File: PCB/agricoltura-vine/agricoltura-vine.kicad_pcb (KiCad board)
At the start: 4 copper layers, 110 x 75 mm, 100 parts, among them SW1 TL3301NF260QG, T1 BU2032SM-JJ-GTR, T10 BM04B-SRSS-TB(LF)(SN), T11 BM04B-SRSS-TB(LF)(SN), T12 BM04B-SRSS-TB(LF)(SN), T13 BM04B-SRSS-TB(LF)(SN), T14 BM04B-SRSS-TB(LF)(SN), T15 BM04B-SRSS-TB(LF)(SN), T16 1757242, T17 0395121004, T18 0395121004, T19 TSW-108-07-G-T, T2 20021121-00010C4LF, T20 TSW-108-07-G-T, T3 0675031020, T4 BM04B-SRSS-TB(LF)(SN), T5 BM04B-SRSS-TB(LF)(SN), T6 BM04B-SRSS-TB(LF)(SN), T7 BM04B-SRSS-TB(LF)(SN), T8 BM04B-SRSS-TB(LF)(SN), T9 BM04B-SRSS-TB(LF)(SN), U1 STM32F446RET6, U2 74HC4052D, U3 TCA9548APWR, U4 AP63203WU-7, U5 AP63205WU-7, U6 MAX13450EAUD+, U7 MAX13450EAUD+, U8 SN74LV541APWR, U9 TXB0108PWR, X1 ABM3B-8.000MHZ-B2-T, X2 ABS07-32.768KHZ-9-T

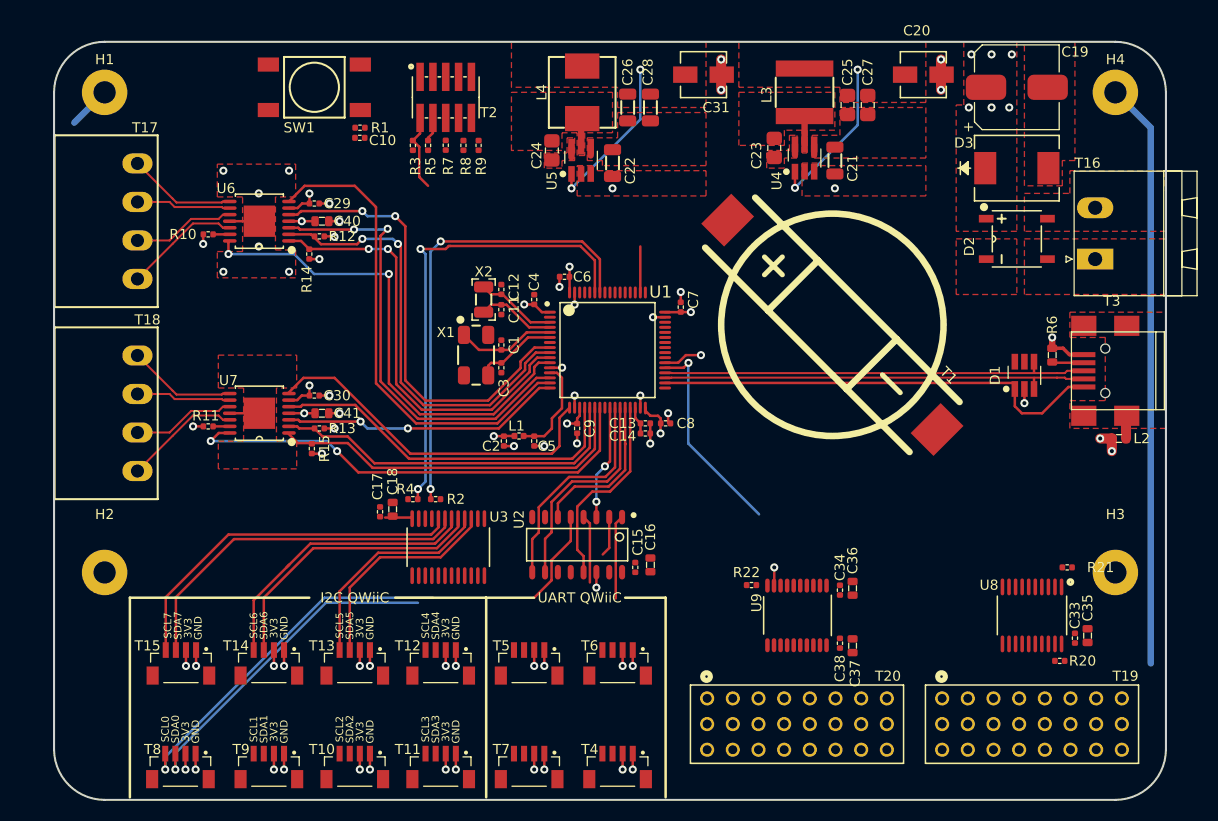
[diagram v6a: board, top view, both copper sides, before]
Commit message: IO Expander
added IO expander for 5V IOs
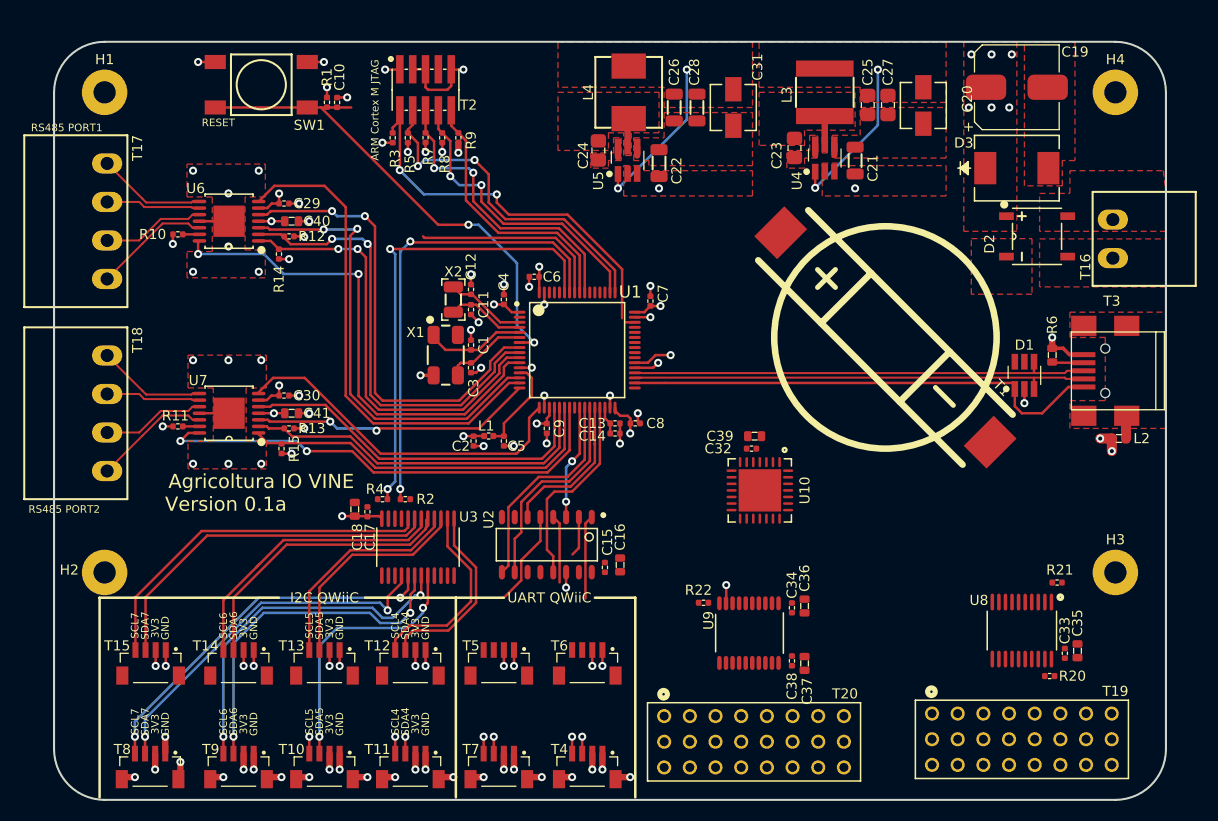
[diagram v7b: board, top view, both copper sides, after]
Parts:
- added C32: C0402C104K9PACTU, AVR-KiCAD-Lib-Resistors:R0402, F.Cu at (174.0, 102.8)
- added C39: GRM188R61A106KE69J, AVR-KiCAD-Lib-Capacitors:C0603, F.Cu at (174.3, 101.5)
- added U10: MCP23017T-E_ML, AVR-KiCAD-Lib-ICs:MCP23017T-E, F.Cu at (174.8, 106.9)
- T16: value 1757242 -> 0395121002; footprint AVR-KiCAD-Lib-Connectors:PhoenixContact_MSTBA-G_02x5.08mm_Angled -> AVR-KiCAD-Lib-Connectors:0395121002
- moved T1 5.40 mm to (187.2, 91.8)
- moved SW1 5.26 mm to (125.5, 66.8)
- moved C34 5.06 mm to (178.0, 118.5)
- moved C36 5.06 mm to (179.2, 118.3)
- moved C37 5.06 mm to (179.2, 124.0)
- moved C38 5.06 mm to (178.0, 123.8)
- moved R22 5.06 mm to (169.2, 118.0)
- moved U9 5.06 mm to (173.8, 121.0)
- moved C22 4.60 mm to (164.8, 74.5)
- moved C24 4.60 mm to (158.8, 73.2)
- moved C26 4.60 mm to (166.3, 69.0)
- moved C28 4.60 mm to (168.6, 69.0)
- moved L4 4.60 mm to (161.8, 67.5)
- moved U5 4.60 mm to (161.7, 74.2)
- moved T20 4.60 mm to (174.2, 131.8)
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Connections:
- net /5V IO Interfaces/5VGPIO_BD_0 renamed Net-(U9-Pad1)
- net /5V IO Interfaces/5VGPIO_BD_1 renamed Net-(U9-Pad3)
- net /5V IO Interfaces/5VGPIO_BD_2 renamed Net-(U9-Pad4)
- net /5V IO Interfaces/5VGPIO_BD_3 renamed Net-(U9-Pad5)
- net /5V IO Interfaces/5VGPIO_BD_4 renamed Net-(U9-Pad6)
- net /5V IO Interfaces/5VGPIO_BD_5 renamed Net-(U9-Pad7)
- net /5V IO Interfaces/5VGPIO_BD_6 renamed Net-(U9-Pad8)
- U1 pad 37: /5V IO Interfaces/5VGPIO_BD_7 -> /STM32F446RET Controller/5VGPIO_BD_7
- U9 pad 9: /5V IO Interfaces/5VGPIO_BD_7 -> Net-(U9-Pad9)
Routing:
- net Earth: track 62.2 -> 249.2 mm
- net /STM32F446RET Controller/NRST: track 0.00 -> 49.2 mm, vias 0 -> 2
- net /I2C Sensor Interfaces/QWIIC_SC1: track 0.00 -> 35.0 mm, vias 0 -> 2
- net /I2C Sensor Interfaces/QWIIC_SD1: track 0.00 -> 34.4 mm, vias 0 -> 2
- net /STM32F446RET Controller/SWDIO_TMS: track 7.64 -> 40.7 mm, vias 0 -> 2
- net /STM32F446RET Controller/SWCLK_TCK: track 2.44 -> 34.2 mm, vias 0 -> 2
- net GND: track 61.2 -> 93.0 mm, vias 44 -> 68
- net /STM32F446RET Controller/SWO_TDO: track 0.00 -> 30.0 mm, vias 0 -> 2
- net /STM32F446RET Controller/NJTRST: track 0.00 -> 26.7 mm
- net /I2C Sensor Interfaces/QWIIC_SD2: track 0.00 -> 26.1 mm, vias 0 -> 2
- net /STM32F446RET Controller/SWO_TDI: track 4.55 -> 29.7 mm, vias 0 -> 2
- net /5V IO Interfaces/5VGPIO_BD_7: track 22.2 -> 0.00 mm, vias 2 -> 0
- net /STM32F446RET Controller/I2C_MUX1_RESET: track 0.00 -> 19.4 mm
- net /I2C Sensor Interfaces/QWIIC_SC4: track 0.00 -> 19.2 mm
- net /I2C Sensor Interfaces/QWIIC_SD4: track 0.00 -> 18.8 mm
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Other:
- board text added: "ARM Cortex M JTAG"
- board text added: "Agricoltura IO VINE"
- board text added: "Agricoltura IO Vine, June 2020"
- board text added: "Designed By Adam Vadala-Roth"
- board text added: "RESET"
- board text added: "RS485 PORT1"
- board text added: "RS485 PORT2"
- board text added: "RS485 Sensing And Control"
- board text added: "Version 0.1a"
- board text removed: "SCL0"
- board text removed: "SCL1"
- board text removed: "SCL2"
- board text removed: "SCL3"
- board text removed: "SDA0"
- board text removed: "SDA1"
- board text removed: "SDA2"
- board text removed: "SDA3"

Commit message: Big Update
Dropped 8 5V outputs in favor of two relays. Ditched microchip IO expander for a Ti one that does level conversion for outputs, eliminates Ti bidriectional converter and 74 line driver from design, simplifying everything.
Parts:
- removed C36, C37, C39: GRM188R61A106KE69J, AVR-KiCAD-Lib-Capacitors:C0603
- removed C38: C0402C104K9PACTU, AVR-KiCAD-Lib-Resistors:R0402
- removed R20, R21, R22: RC0402FR-071KL, AVR-KiCAD-Lib-Resistors:R0402
- removed T20: TSW-108-07-G-T, AVR-KiCAD-Lib-Connectors:TSW-108-07-G-T
- removed U10: MCP23017T-E_ML, AVR-KiCAD-Lib-ICs:MCP23017T-E
- removed U9: TXB0108PWR, AVR-KiCAD-Lib-ICs:TXB0108PWR
- added K1: G5LE-14_DC5, AVR-KiCAD-Lib-Relays-Contactors:G5LE-14_DC5, F.Cu at (173.5, 117.2)
- added K2: G5LE-14_DC5, AVR-KiCAD-Lib-Relays-Contactors:G5LE-14_DC5, F.Cu at (191.8, 117.2)
- added T22: 0395121006, AVR-KiCAD-Lib-Connectors:0395121006, F.Cu at (182.8, 132.0)
- C33: value C0402C104K9PACTU -> GRM188R61A106KE69J; footprint AVR-KiCAD-Lib-Resistors:R0402 -> AVR-KiCAD-Lib-Capacitors:C0603
- U8: value SN74LV541APWR -> TCA6416ARTWR; footprint AVR-KiCAD-Lib-ICs:SN74LVC541APWR -> AVR-KiCAD-Lib-ICs:TCA6416ARTWR
- moved C35 52.1 mm to (167.7, 87.8)
- moved C33 47.7 mm to (167.8, 93.2), turned to 270 degrees
- moved U8 41.0 mm to (172.5, 91.0), turned to 90 degrees
- moved C34 31.7 mm to (169.0, 88.1)
- moved T19 19.4 mm to (210.5, 114.8), turned to 270 degrees
- moved H3 17.5 mm to (210.0, 130.0)
- moved C16 13.8 mm to (147.8, 110.5), turned to 270 degrees
- moved C15 11.1 mm to (149.2, 110.2), turned to 270 degrees
- moved C32 11.0 mm to (169.0, 93.0), turned to 270 degrees
- moved T7 8.75 mm to (157.8, 134.5)
- moved T4 8.75 mm to (149.0, 134.2)
- moved U2 1.27 mm to (155.0, 112.5), turned to 90 degrees
- moved C17 0.50 mm to (136.0, 109.5)
- moved C18 0.50 mm to (134.8, 109.2)
- moved T1 0.35 mm to (187.0, 91.5)
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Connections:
- C33 pad 1: +5V -> +3V3
- C34 pad 1: +3V3 -> +5V
- R2 pad 2: /STM32F446RET Controller/I2C_SENSE1_SCL -> /I2C Sensor Interfaces/I2C_SENSE1_SCL
- R4 pad 2: /STM32F446RET Controller/I2C_SENSE1_SDA -> /I2C Sensor Interfaces/I2C_SENSE1_SDA
- U1 pad 26: /STM32F446RET Controller/USW1_S1 -> /STM32F446RET Controller/USW1_EN
- U1 pad 28: /STM32F446RET Controller/USW1_EN -> /STM32F446RET Controller/USW1_S1
- U1 pad 57: /STM32F446RET Controller/I2C_MUX1_RESET -> /I2C Sensor Interfaces/I2C_MUX1_RESET
- U1 pad 58: /STM32F446RET Controller/I2C_SENSE1_SCL -> /I2C Sensor Interfaces/I2C_SENSE1_SCL
- U1 pad 59: /STM32F446RET Controller/I2C_SENSE1_SDA -> /I2C Sensor Interfaces/I2C_SENSE1_SDA
- U8 pad 10: GND -> Net-(T19-Pad1)
- U8 pad 11: Net-(T19-Pad1) -> Net-(T19-Pad4)
- U8 pad 12: Net-(T19-Pad4) -> Net-(T19-Pad7)
- U8 pad 13: Net-(T19-Pad7) -> Net-(T19-Pad10)
- U8 pad 14: Net-(T19-Pad10) -> Net-(T19-Pad13)
- U8 pad 15: Net-(T19-Pad13) -> Net-(T19-Pad16)
- U8 pad 16: Net-(T19-Pad16) -> Net-(T19-Pad19)
- U8 pad 17: Net-(T19-Pad19) -> Net-(T19-Pad22)
- U8 pad 18: Net-(T19-Pad22) -> Net-(U8-Pad18)
- U8 pad 19: Net-(R20-Pad2) -> /5V IO Interfaces/IO_SCL
- U8 pad 20: +5V -> /5V IO Interfaces/IO_SDA
- U8 pad 9: Net-(U10-Pad17) -> GND
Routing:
- net Earth: track 249.2 -> 101.0 mm
- net /I2C Sensor Interfaces/I2C_MUX1_RESET: track 0.00 -> 63.5 mm, vias 0 -> 2
- net /I2C Sensor Interfaces/I2C_SENSE1_SDA: track 0.00 -> 48.3 mm, vias 0 -> 2
- net /I2C Sensor Interfaces/I2C_SENSE1_SCL: track 0.00 -> 47.9 mm, vias 0 -> 2
- net /STM32F446RET Controller/I2C_SENSE1_SDA: track 46.2 -> 0.00 mm, vias 2 -> 0
- net /STM32F446RET Controller/I2C_SENSE1_SCL: track 45.7 -> 0.00 mm, vias 2 -> 0
- net GND: track 93.0 -> 127.7 mm, vias 68 -> 85
- net /STM32F446RET Controller/VBAT: track 2.85 -> 29.9 mm
- net /UART Sensor Interfaces/UARTS1_TX: track 1.68 -> 28.3 mm, vias 1 -> 2
- net /I2C Sensor Interfaces/QWIIC_SC2: track 1.68 -> 27.9 mm, vias 1 -> 2
- net Net-(K1-Pad1): track 0.00 -> 24.3 mm
- net Net-(K2-Pad1): track 0.00 -> 24.2 mm
- net /UART Sensor Interfaces/UARTS4_RX: track 1.68 -> 25.1 mm, vias 1 -> 2
- net /UART Sensor Interfaces/UARTS3_RX: track 0.00 -> 22.2 mm, vias 0 -> 2
- net /STM32F446RET Controller/I2C_MUX1_RESET: track 19.4 -> 0.00 mm
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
